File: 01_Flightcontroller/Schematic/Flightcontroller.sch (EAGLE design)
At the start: 36 parts, among them IC1 FT232RL, IC2 MPU6000, J1 2908-05WB-MG, U1 STM32F7X2RXT, U2 ATMEGA328P_TQFP, U3 LM3940IMPX-3.3/NOPB, Y1 8MHz, Y2 16MHz

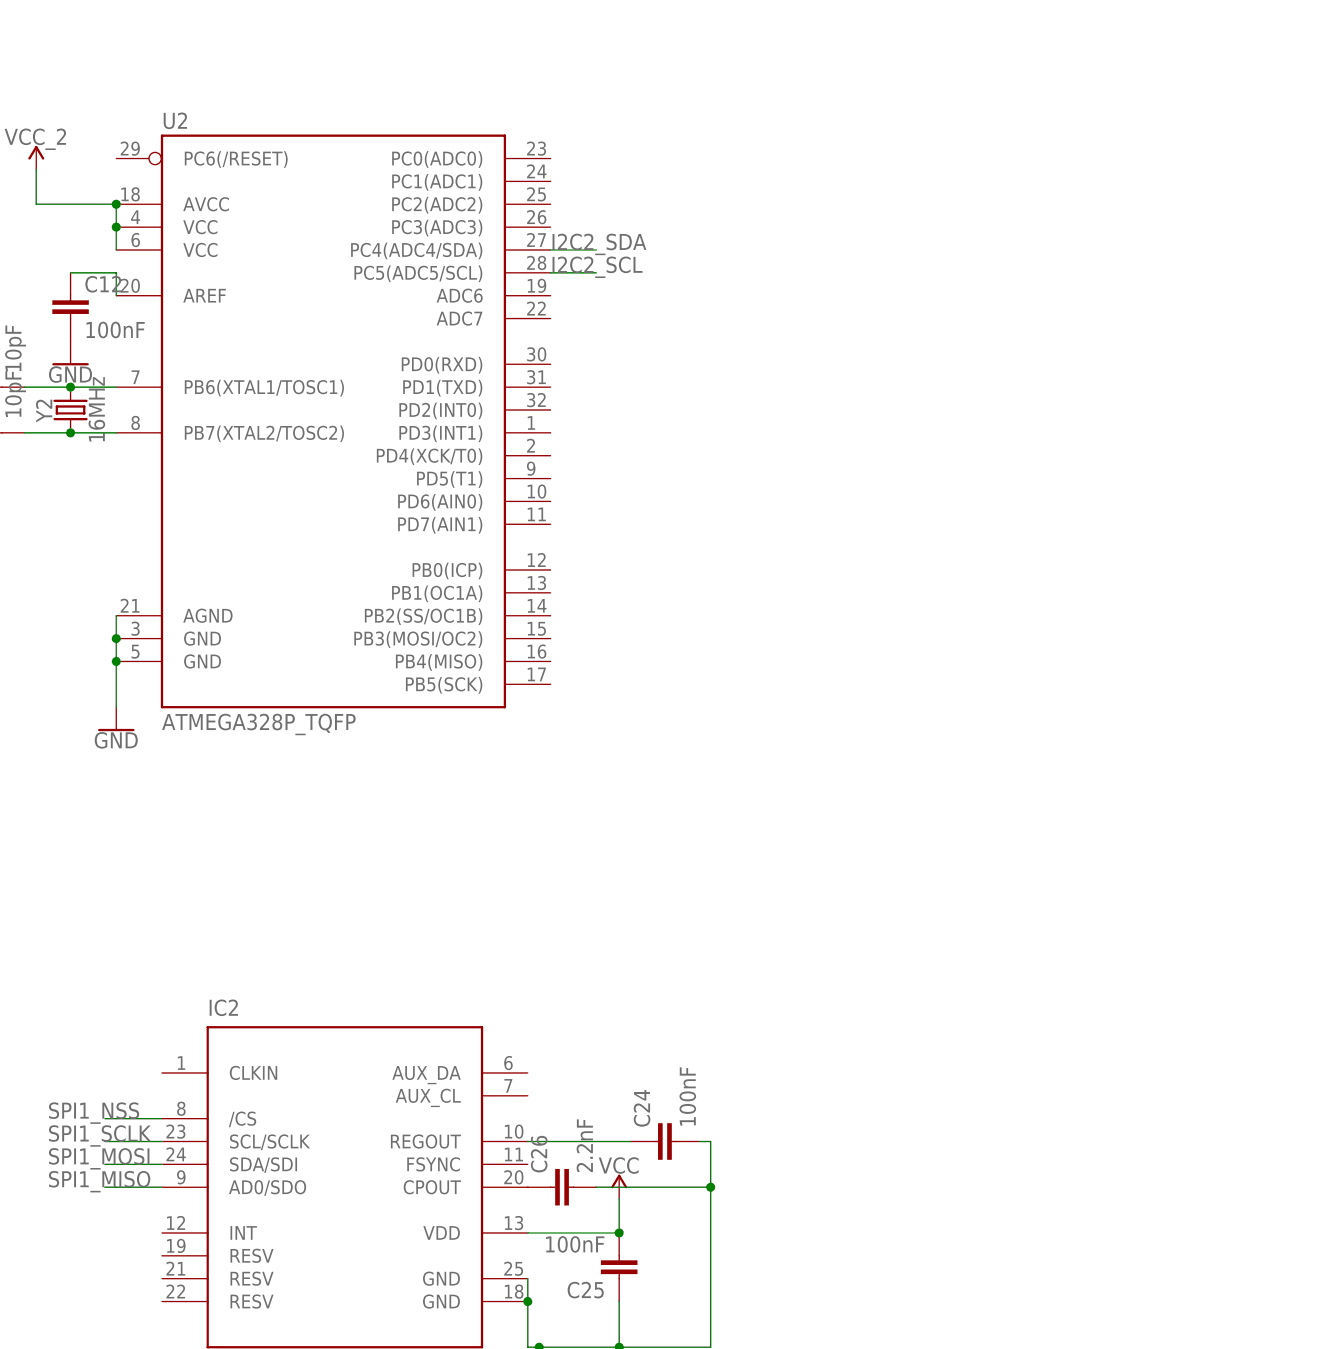
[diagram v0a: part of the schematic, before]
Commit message: Hinzufügen des BMP280 -> ändern auf 3V3 LOGIK mit Chip oder Mosfet
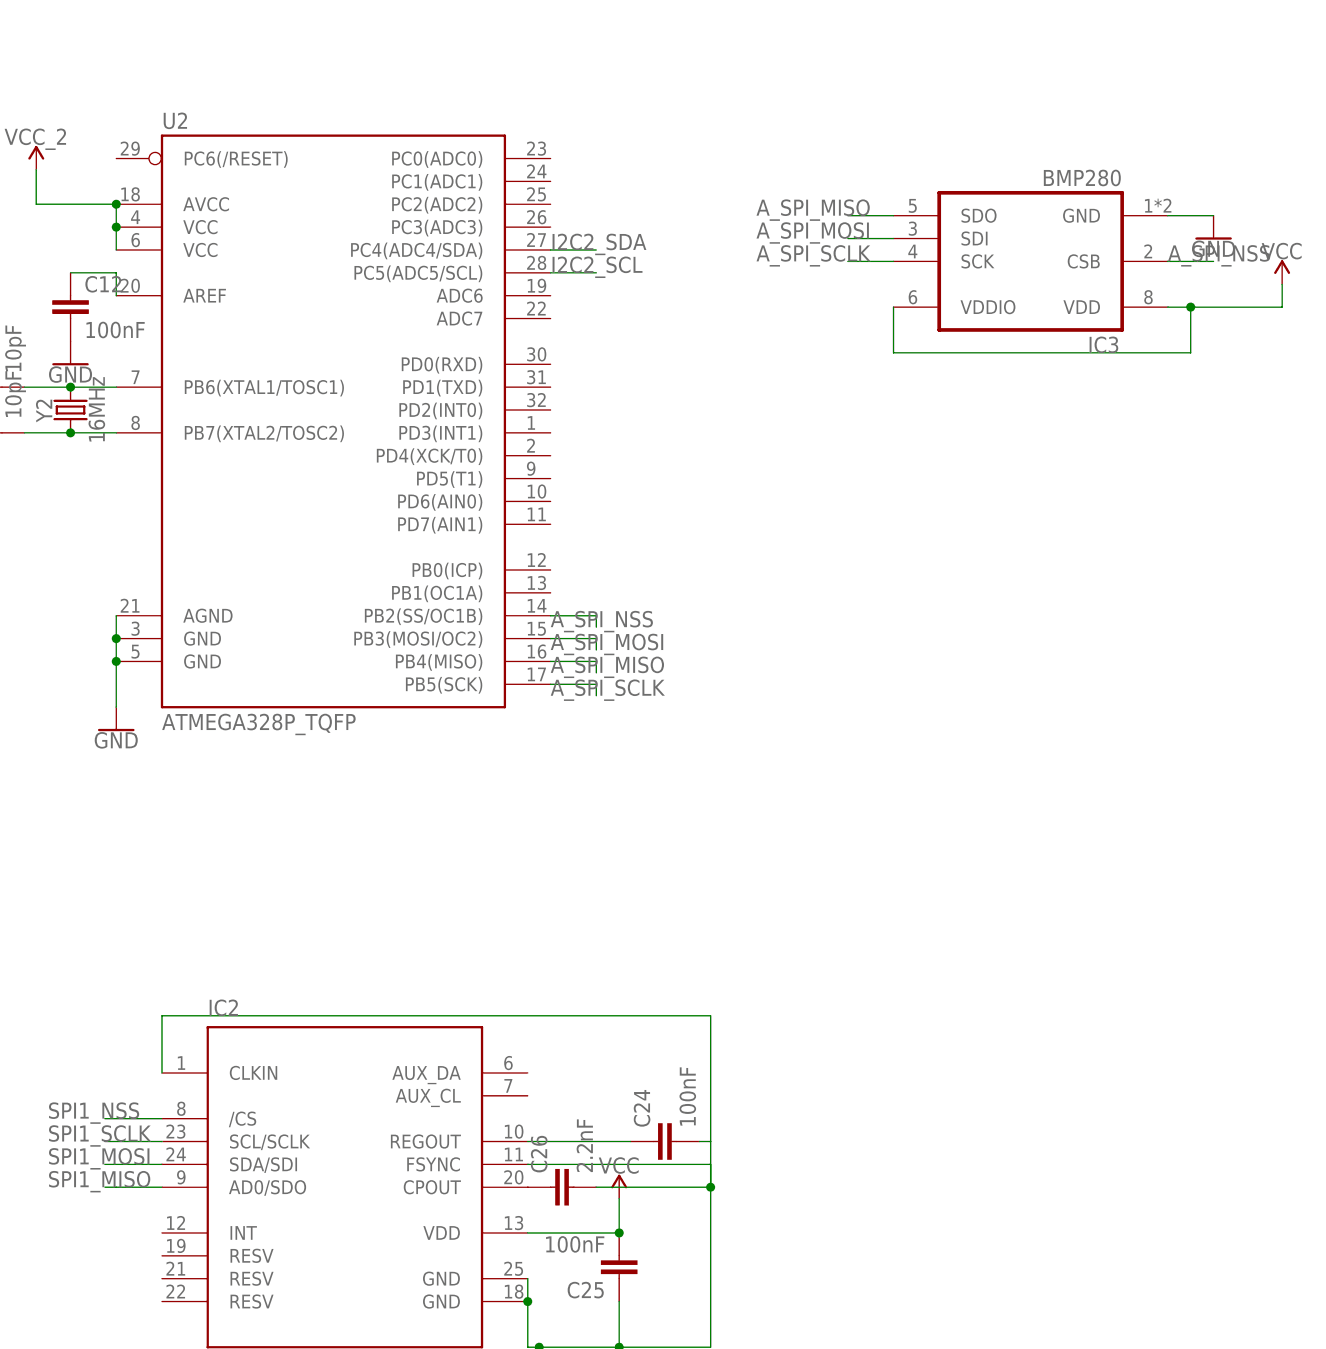
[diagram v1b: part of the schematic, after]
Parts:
- added IC3: BMP280, bosch-bmp280:BMP280
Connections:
- new net A_SPI_MISO: IC3.SDO, U2.PB4(MISO)
- new net A_SPI_MOSI: IC3.SDI, U2.PB3(MOSI/OC2)
- new net A_SPI_NSS: IC3.CSB, U2.PB2(SS/OC1B)
- new net A_SPI_SCLK: IC3.SCK, U2.PB5(SCK)
- net GND: now also IC2G$1.CLKIN, IC2G$1.FSYNC, IC3.GND
- net VCC: now also IC3.VDD, IC3.VDDIO
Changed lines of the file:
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@@
 <part name="GND14" library="SparkFun-PowerSymbols" library_urn="urn:adsk.eagle:library:530" deviceset="GND" device=""/>
 <part name="C27" library="resistor" library_urn="urn:adsk.eagle:library:348" deviceset="C-EU" device="C1206" package3d_urn="urn:adsk.eagle:package:23618/2" value="4.7uF"/>
+<part name="IC3" library="bosch-bmp280" deviceset="BMP280" device=""/>
+<part name="SUPPLY16" library="SparkFun-PowerSymbols" library_urn="urn:adsk.eagle:library:530" deviceset="VCC" device=""/>
+<part name="GND15" library="SparkFun-PowerSymbols" library_urn="urn:adsk.eagle:library:530" deviceset="GND" device=""/>
 </parts>
 <sheets>
@@
 <attribute name="NAME" x="-44.196" y="53.721" size="1.778" layer="95"/>
 <attribute name="VALUE" x="-44.196" y="48.641" size="1.778" layer="96"/>
+</instance>
+<instance part="IC3" gate="G$1" x="266.7" y="66.04" smashed="yes" rot="R180">
+<attribute name="NAME" x="276.606" y="57.658" size="1.778" layer="95" font="vector" rot="R180"/>
+<attribute name="VALUE" x="276.86" y="76.2" size="1.778" layer="96" font="vector" rot="R180"/>
+</instance>
+<instance part="SUPPLY16" gate="G$1" x="294.64" y="63.5" smashed="yes">
+<attribute name="VALUE" x="294.64" y="66.294" size="1.778" layer="96" align="bottom-center"/>
+</instance>
+<instance part="GND15" gate="1" x="287.02" y="68.58" smashed="yes">
+<attribute name="VALUE" x="287.02" y="68.326" size="1.778" layer="96" align="top-center"/>
 </instance>
 </instances>
@@
 <wire x1="218.44" y1="-36.83" x2="231.14" y2="-36.83" width="0.1524" layer="91"/>
 <junction x="231.14" y="-36.83"/>
+<pinref part="IC2" gate="G$1" pin="FSYNC"/>
+<wire x1="210.82" y1="-34.29" x2="231.14" y2="-34.29" width="0.1524" layer="91"/>
+<wire x1="231.14" y1="-34.29" x2="231.14" y2="-36.83" width="0.1524" layer="91"/>
+<pinref part="IC2" gate="G$1" pin="CLKIN"/>
+<wire x1="170.18" y1="-24.13" x2="170.18" y2="-17.78" width="0.1524" layer="91"/>
+<wire x1="170.18" y1="-17.78" x2="231.14" y2="-17.78" width="0.1524" layer="91"/>
+<wire x1="231.14" y1="-17.78" x2="231.14" y2="-31.75" width="0.1524" layer="91"/>
 </segment>
 <segment>
@@
 <wire x1="-45.72" y1="48.26" x2="-45.72" y2="44.45" width="0.1524" layer="91"/>
 <junction x="-45.72" y="44.45"/>
+</segment>
+<segment>
+<pinref part="IC3" gate="G$1" pin="GND"/>
+<pinref part="GND15" gate="1" pin="GND"/>
+<wire x1="281.94" y1="71.12" x2="287.02" y2="71.12" width="0.1524" layer="91"/>
 </segment>
 </net>
@@
 <junction x="-45.72" y="59.69"/>
 </segment>
+<segment>
+<pinref part="SUPPLY16" gate="G$1" pin="VCC"/>
+<pinref part="IC3" gate="G$1" pin="VDD"/>
+<wire x1="294.64" y1="63.5" x2="294.64" y2="60.96" width="0.1524" layer="91"/>
+<wire x1="294.64" y1="60.96" x2="284.48" y2="60.96" width="0.1524" layer="91"/>
+<pinref part="IC3" gate="G$1" pin="VDDIO"/>
+<wire x1="284.48" y1="60.96" x2="281.94" y2="60.96" width="0.1524" layer="91"/>
+<wire x1="251.46" y1="60.96" x2="251.46" y2="55.88" width="0.1524" layer="91"/>
+<wire x1="251.46" y1="55.88" x2="284.48" y2="55.88" width="0.1524" layer="91"/>
+<wire x1="284.48" y1="55.88" x2="284.48" y2="60.96" width="0.1524" layer="91"/>
+<junction x="284.48" y="60.96"/>
+</segment>
 </net>
 <net name="N$2" class="0">
@@
 </segment>
 </net>
+<net name="A_SPI_SCLK" class="0">
+<segment>
+<pinref part="U2" gate="U$1" pin="PB5(SCK)"/>
+<wire x1="213.36" y1="19.05" x2="218.44" y2="19.05" width="0.1524" layer="91"/>
+<wire x1="218.44" y1="19.05" x2="218.44" y2="17.78" width="0.1524" layer="91"/>
+<label x="213.36" y="17.78" size="1.778" layer="95"/>
+</segment>
+<segment>
+<pinref part="IC3" gate="G$1" pin="SCK"/>
+<wire x1="251.46" y1="66.04" x2="246.38" y2="66.04" width="0.1524" layer="91"/>
+<label x="236.22" y="66.04" size="1.778" layer="95"/>
+</segment>
+</net>
+<net name="A_SPI_MISO" class="0">
+<segment>
+<pinref part="U2" gate="U$1" pin="PB4(MISO)"/>
+<wire x1="213.36" y1="21.59" x2="218.44" y2="21.59" width="0.1524" layer="91"/>
+<wire x1="218.44" y1="21.59" x2="218.44" y2="20.32" width="0.1524" layer="91"/>
+<label x="213.36" y="20.32" size="1.778" layer="95"/>
+</segment>
+<segment>
+<pinref part="IC3" gate="G$1" pin="SDO"/>
+<wire x1="251.46" y1="71.12" x2="246.38" y2="71.12" width="0.1524" layer="91"/>
+<label x="236.22" y="71.12" size="1.778" layer="95"/>
+</segment>
+</net>
+<net name="A_SPI_MOSI" class="0">
+<segment>
+<pinref part="U2" gate="U$1" pin="PB3(MOSI/OC2)"/>
+<wire x1="213.36" y1="24.13" x2="218.44" y2="24.13" width="0.1524" layer="91"/>
+<wire x1="218.44" y1="24.13" x2="218.44" y2="22.86" width="0.1524" layer="91"/>
+<label x="213.36" y="22.86" size="1.778" layer="95"/>
+</segment>
+<segment>
+<pinref part="IC3" gate="G$1" pin="SDI"/>
+<wire x1="251.46" y1="68.58" x2="246.38" y2="68.58" width="0.1524" layer="91"/>
+<label x="236.22" y="68.58" size="1.778" layer="95"/>
+</segment>
+</net>
+<net name="A_SPI_NSS" class="0">
+<segment>
+<pinref part="U2" gate="U$1" pin="PB2(SS/OC1B)"/>
+<wire x1="213.36" y1="26.67" x2="218.44" y2="26.67" width="0.1524" layer="91"/>
+<wire x1="218.44" y1="26.67" x2="218.44" y2="25.4" width="0.1524" layer="91"/>
+<label x="213.36" y="25.4" size="1.778" layer="95"/>
+</segment>
+<segment>
+<pinref part="IC3" gate="G$1" pin="CSB"/>
+<wire x1="281.94" y1="66.04" x2="287.02" y2="66.04" width="0.1524" layer="91"/>
+<label x="281.94" y="66.04" size="1.778" layer="95"/>
+</segment>
+</net>

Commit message: Hinzufügen LogicLevelShifter
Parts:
- added C28, C29: 100nF, rcl:C-EUC1206
- added R1: 10k, SparkFun-Resistors:10KOHM-0603-1/10W-1%
- added R2, R3, R4, R5: 4.7k, SparkFun-Resistors:4.7KOHM-0603-1/10W-1%
- added U4: TXB0104, SparkFun-IC-Comms:TXB0104PWRSOIC14
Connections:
- removed net VDD: U1B.VDD, U1B.VDDA, U1B.VDD_2, U1B.VDD_3, U1B.VDD_4
- new net B_SPI_MISO: IC3.SDO, U4.A2
- new net B_SPI_MOSI: IC3.SDI, U4.A3
- new net B_SPI_NSS: IC3.CSB, U4.A4
- new net B_SPI_SCLK: IC3.SCK, U4.A1
- new net LLVOE: R1.2, U4.OE
- new net N$12: R5.1
- net A_SPI_MISO: now also U4.B2; no longer IC3.SDO
- net A_SPI_MOSI: now also U4.B3; no longer IC3.SDI
- net A_SPI_NSS: now also U4.B4; no longer IC3.CSB
- net A_SPI_SCLK: now also U4.B1; no longer IC3.SCK
- net GND: now also C28.1, C29.1, R1.1, U4.GND
- net I2C1_SCL: now also R4.1
- net I2C2_SCL: now also R3.1
- net I2C2_SDA: now also R2.1
- net VCC: now also C29.2, R2.2, R3.2, R4.2, R5.2, U1B.VDD, U1B.VDDA, U1B.VDD_2, U1B.VDD_3, U1B.VDD_4, U4.VCCA
- net VCC_2: now also C28.2, U4.VCCB

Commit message: -Schaltung hinzufügen von Pins und Wiederständen -Schriftlicher Teil Hinzfügen von Bauteil des Flightconrollers.
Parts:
- added C30, C31: 100nF, rcl:C-EUC1206
- added GIMBAL_X, GIMBAL_Y, GIMBAL_Z, JP1, JP2, LED_STRIPES, M1, M2, M3, M4: (no value), adafruit:PINHD-1X3
- added GPS, OSD, SONIC1, SONIC2, SONIC3, SONIC4, SONIC5, SONIC6: 1X4-BIG, adafruit:1X4-BIG
- added ISP1: AVRISP-6, adafruit:AVRISP-6
- added JP3: (no value), adafruit:PINHD-1X8CLEANBIG
- added JP4: (no value), adafruit:PINHD-1X6
- added LED1, LED2, LED3, LED4, LED5, LED6: (no value), adafruit:LEDSMT1206
- added R10, R11, R12, R7, R8, R9: 1k, SparkFun-Resistors:10KOHM-0603-1/10W-1%
- added R6: 10k, SparkFun-Resistors:10KOHM-0603-1/10W-1%
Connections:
- net N$13 renamed CE
- new net ADC1: JP1.1, U2.ADC6
- new net ADC2: JP2.1, U2.ADC7
- new net BATTSENS: U1A.PA6
- new net CS: U1A.PC6
- new net DAC_OUT: U1A.PA5
- new net DRDY: JP3.1
- new net ECHO1_IN: SONIC1.3, U2.PD1(TXD)
- new net ECHO2_IN: SONIC2.3, U2.PC1(ADC1)
- new net ECHO3_IN: SONIC3.3, U2.PC3(ADC3)
- new net ECHO4_IN: SONIC4.3, U2.PD4(XCK/T0)
- new net ECHO5_IN: SONIC5.3, U2.PD6(AIN0)
- new net ECHO6_IN: SONIC6.3, U2.PB0(ICP)
- new net FSYNC: JP3.3
- new net GIMBAL_X: GIMBAL_X.1, U1A.PB4
- new net GIMBAL_Y: GIMBAL_Y.1, U1A.PB5
- new net GIMBAL_Z: GIMBAL_Z.1, U1A.PB0
- new net IMU_INT: IC2G$1.INT, U1A.PB9
- new net INIT_OK: LED5.A, U1A.PA7
- new net INTA: JP3.2, U1A.PB8
- new net IRQ: U$1.IRQ, U1A.PC7
- new net LED: LED_STRIPES.2, U2.PB1(OC1A)
- new net LED_RX: IC1.CBUS0, R8.1
- new net LED_TX: IC1.CBUS1, R7.1
- new net MOD0_LED: LED3.A, U1A.PC4
- new net MOD1_LED: LED4.A, U1A.PB1
- new net N$13: LED1.C, R7.2
- new net N$14: LED2.C, R8.2
- new net N$15: LED3.C, R9.2
- new net N$16: LED4.C, R10.2
- new net N$17: LED5.C, R11.2
- new net N$18: LED6.C, R12.2
- new net N$8: R6.2, U1A.BOOT0
- new net N$9: C31.1, IC1.!RESET
- new net PPM_IN: U2.PD2(INT0)
- new net PWM_1: M1.1, U1A.PA0-WKUP
- new net PWM_2: M2.1, U1A.PA1
- new net PWM_3: M3.1, U1A.PB10
- new net PWM_4: M4.1, U1A.PB11
- new net RST: C30.1, C31.2, ISP1.RST, JP4.5, U1A.NRST, U2.PC6(/RESET)
- new net TRIGG1_IN: SONIC1.2, U2.PD0(RXD)
- new net TRIGG2_IN: SONIC2.2, U2.PC0(ADC0)
- new net TRIGG3_IN: SONIC3.2, U2.PC2(ADC2)
- new net TRIGG4_IN: SONIC4.2, U2.PD3(INT1)
- new net TRIGG5_IN: SONIC5.2, U2.PD5(T1)
- new net TRIGG6_IN: SONIC6.2, U2.PD7(AIN1)
- new net USBOSD: U1A.PA12
- net A_SPI_MISO: now also ISP1.MISO
- net A_SPI_MOSI: now also ISP1.MOSI
- net A_SPI_SCLK: now also ISP1.SCK
- net GND: now also C30.2, GIMBAL_X.3, GIMBAL_Y.3, GIMBAL_Z.3, GPS.2, ISP1.GND, JP1.3, JP2.3, JP3.6, JP4.3, LED_STRIPES.3, M1.3, M2.3, M3.3, M4.3, OSD.2, R10.1, R11.1, R12.1, R6.1, R9.1, SONIC1.4, SONIC2.4, SONIC3.4, SONIC4.4, SONIC5.4, SONIC6.4
- net I2C1_SCL: now also JP3.5
- net I2C1_SDA: now also JP3.4
- net I2C2_SCL: now also U1A.PA8; no longer U1A.PB10
- net I2C2_SDA: now also U1A.PC9; no longer U1A.PB11
- net LLVOE: now also U1A.PA11
- net SPI1_MISO: now also U1A.PC11; no longer U1A.PA6
- net SPI1_MOSI: now also U1A.PB2; no longer U1A.PA7
- net SPI1_SCLK: now also U1A.PC10; no longer U1A.PA5
- net SWCLK: now also JP4.2
- net SWDIO: now also JP4.4
- net SWO: now also JP4.6
- net UART1_RX: now also OSD.3
- net UART1_TX: now also OSD.4
- net UART2_RX: now also GPS.3
- net UART2_TX: now also GPS.4
- net VCC: now also GIMBAL_X.2, GIMBAL_Y.2, GIMBAL_Z.2, GPS.1, JP3.7, JP4.1, LED6.A, M1.2, M2.2, M3.2, M4.2, OSD.1
- net VCC_2: now also ISP1.VCC, JP1.2, JP2.2, LED1.A, LED2.A, LED_STRIPES.1, SONIC1.1, SONIC2.1, SONIC3.1, SONIC4.1, SONIC5.1, SONIC6.1
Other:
- moved on the sheet: C24, C26, C28, C29, C8, C9, IC3, R1, R2, R3, R4, R5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

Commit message: Schelmischer Versuch von Board Design 215 Vias :)
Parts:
- added C32, C33: 10uF, rcl:C-EUC1812
- added C34: 1uF, rcl:C-EUC1206
- added C35: 100nF, rcl:C-EUC1206
- added SW1: (no value), adafruit:SWITCH_PUSHBUTTONC&K_KSS
- C22: value 33uF -> 10uF
- C23: value 0.47uF -> 1uF
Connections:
- removed net N$12: R5.1
- net GND: now also C32.2, C33.2, C34.2, C35.2, SW1.P$2
- net I2C1_SDA: now also R5.1
- net RST: now also C35.1, SW1.P$1
- net VCC: now also C32.1, C33.1
- net VCC_2: now also C34.1
